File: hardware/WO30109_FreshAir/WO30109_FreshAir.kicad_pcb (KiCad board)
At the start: 2 copper layers, 63.4 x 83.1 mm, 44 parts, among them K1 G5Q-1 DC12, K2 G5Q-1 DC12, K3 G5Q-1 DC12, K4 G5Q-1 DC12, P1 AC IN, P2 SWD, P3 AC OUT, Q1 Si2302CDS, Q2 Si2302CDS, Q3 Si2302CDS, Q4 Si2302CDS, U1 STM32F103C8T6, U2 IRM-02-12, U3 ZS3L, U4 LM1117-3.3

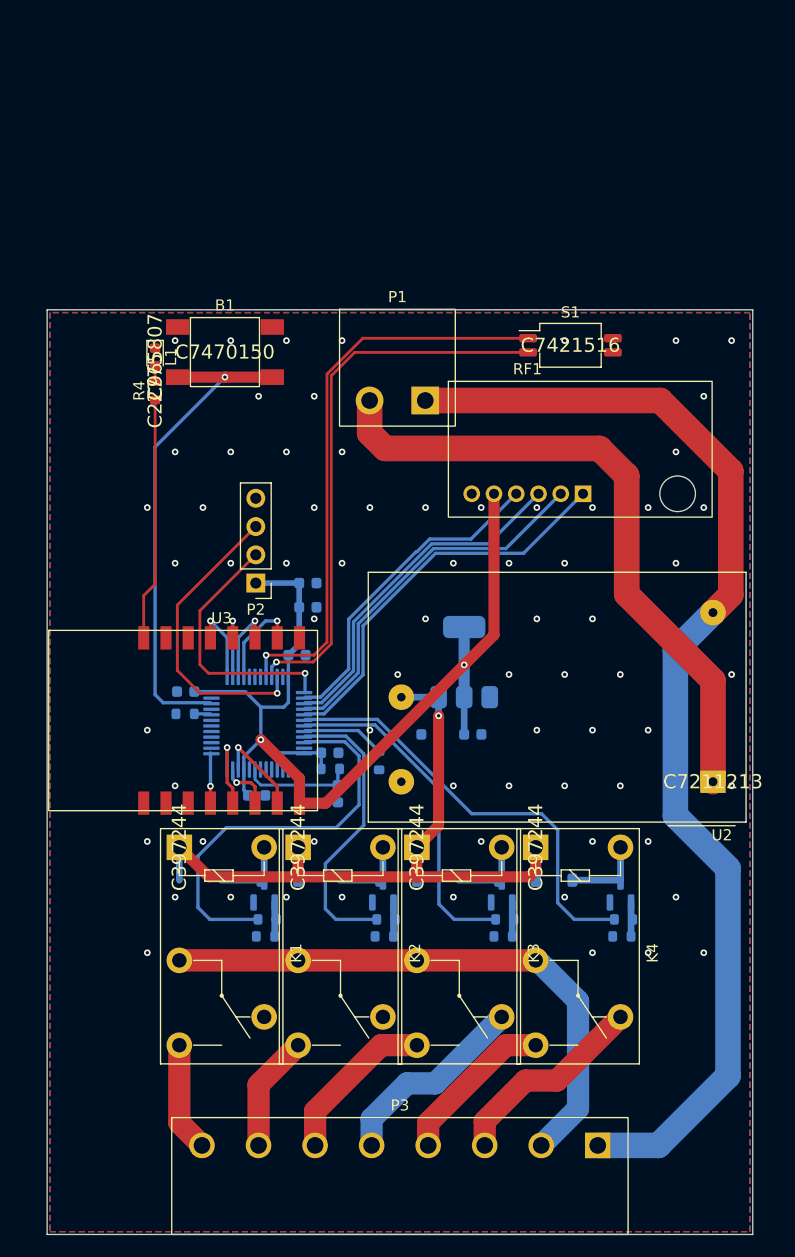
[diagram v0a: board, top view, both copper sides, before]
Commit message: feat(v2.0): PCB 安規改版完成 — DRC 0 錯誤、全部接通
PCB
- 市電↔低壓 ≥6.4mm、市電網路間 ≥1.5mm、板邊 ≥0.5mm（.kicad_dru 規則）
- 新增固定孔到市電 ≥2.3mm 規則；右緣市電走道外移、AC_N 在 H2 旁內彎（H2 0.85→2.85mm）
- F1/RV1、AP63203 降壓、繼電器驅動、RF1/P2/S1 重新擺放；H1–H4 固定孔
- 繼電器輸出 DO_* 由 mains_router 雙層格點佈線；低壓由 Freerouting，剩餘由 route_leftovers 補
- GND 鋪銅依規則自動退讓；LCSC 料號不印絲印

工具與文件
- scripts/build_v20.sh 一鍵重建（多組 Freerouting 設定，取第一組全接通）
- .github/workflows/kicad-ci.yml：ERC/DRC/生產檔
- README：架構、改版、安規、版控、CI、範例（mermaid 圖）＋板子圖片
- docs/review：V1.3 設計審查

驗證（kicad-cli 10.0.6）：ERC 0、DRC 0 錯誤、0 未連線、0 parity

Co-Authored-By: Claude Opus 5.5 (1M context) <noreply@anthropic.com>
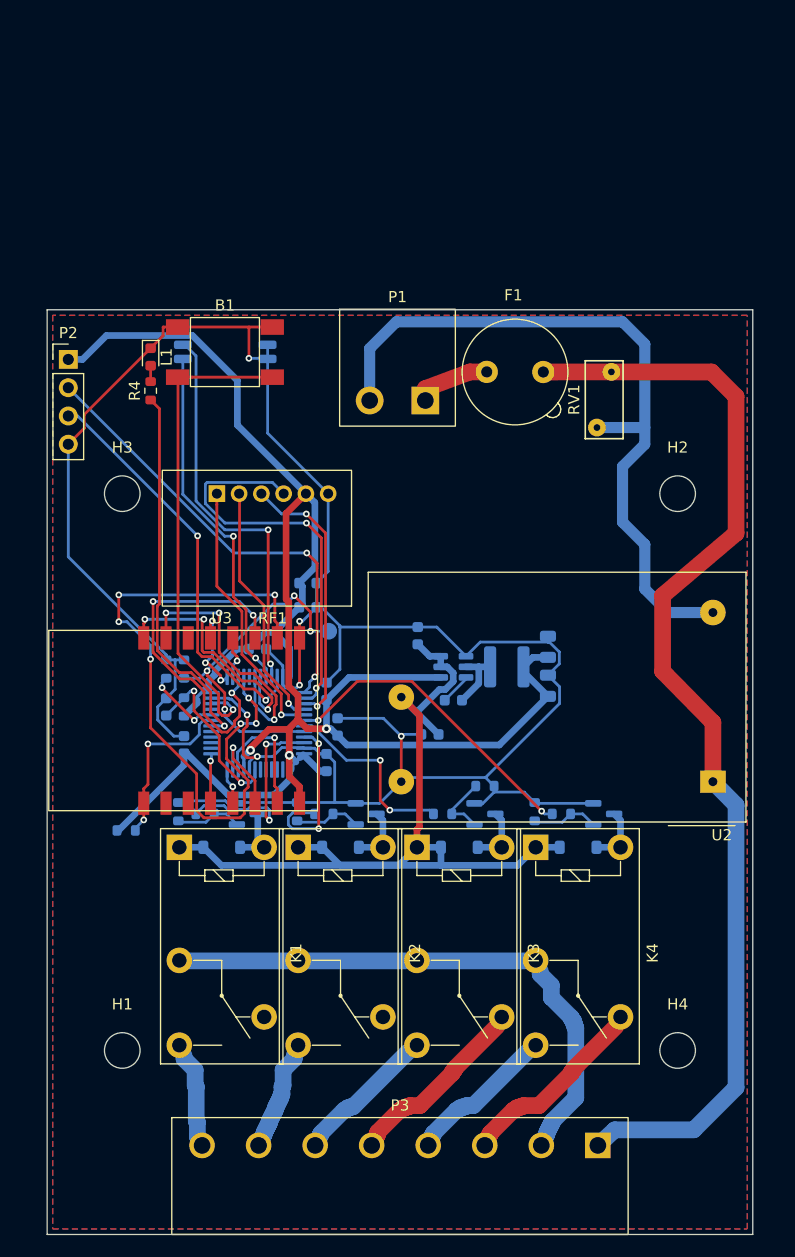
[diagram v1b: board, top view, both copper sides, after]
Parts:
- added C10: 1uF, Capacitor_SMD:C_0603_1608Metric, B.Cu at (112.3, 139.1)
- added C12: 100nF, Capacitor_SMD:C_0603_1608Metric, B.Cu at (136.5, 135.1)
- added C13: 22uF 25V, Capacitor_SMD:C_0805_2012Metric, B.Cu at (145.0, 130.3)
- added C14: 100nF, Capacitor_SMD:C_0603_1608Metric, B.Cu at (133.3, 129.3)
- added F1: T3.15A 250V, Fuse:Fuseholder_TR5_Littelfuse_No560_No460, F.Cu at (139.5, 105.6)
- added H1: M3, MountingHole:MountingHole_3.2mm_M3, F.Cu at (106.8, 166.6)
- added H2: M3, MountingHole:MountingHole_3.2mm_M3, F.Cu at (156.7, 116.5)
- added H3: M3, MountingHole:MountingHole_3.2mm_M3, F.Cu at (106.8, 116.5)
- added H4: M3, MountingHole:MountingHole_3.2mm_M3, F.Cu at (156.7, 166.6)
- added L2: 3.9uH, Inductor_SMD:L_Sunlord_SWPA4030S, B.Cu at (141.3, 132.1)
- added R13: 10k, Resistor_SMD:R_0603_1608Metric, B.Cu at (107.1, 146.8)
- added RV1: 07D471K, Varistor:RV_Disc_D7mm_W3.4mm_P5mm, F.Cu at (150.7, 105.6)
- added TP1: BOOT0, TestPoint:TestPoint_Pad_D1.5mm, B.Cu at (125.3, 128.9)
- C5: value 1uF -> 100nF
- C7: value 10uF -> 22uF 25V; footprint Capacitor_SMD:C_0603_1608Metric -> Capacitor_SMD:C_0805_2012Metric
- K1, K2, K3, K4: footprint Relay_THT:Relay_SPDT_Omron-G5Q-1 -> WOOW:Relay_SPDT_Omron-G5Q-1_Tight
- P1: value AC IN -> AC IN 230V
- S1: moved to B.Cu
- U4: value LM1117-3.3 -> AP63203WU-7; footprint Package_TO_SOT_SMD:SOT-223-3_TabPin2 -> Package_TO_SOT_SMD:TSOT-23-6
- moved S1 31.0 mm to (116.0, 103.8)
- moved P2 26.2 mm to (101.9, 104.5), turned to 0 degrees
- moved RF1 22.9 mm to (120.2, 116.5), turned to 180 degrees
- moved R2 19.4 mm to (112.3, 132.3), turned to 90 degrees
- moved C5 17.3 mm to (110.7, 135.7), turned to 90 degrees
- moved R1 14.3 mm to (112.3, 135.7), turned to 90 degrees
- moved C4 14.2 mm to (125.1, 140.7), turned to 90 degrees
- moved R10 13.7 mm to (122.5, 145.1), turned to 90 degrees
- moved R12 13.7 mm to (143.8, 145.1), turned to 90 degrees
- moved R9 13.7 mm to (111.8, 145.1), turned to 90 degrees
- moved R11 13.6 mm to (139.3, 142.8), turned to 0 degrees
- moved C3 11.3 mm to (125.1, 134.3), turned to 90 degrees
- moved R5 11.0 mm to (114.2, 145.3)
- moved R8 11.0 mm to (146.2, 145.3)
- moved R7 11.0 mm to (135.5, 145.3)
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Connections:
- P1 pad 1: /AC_L -> /AC_L_IN
- R4 pad 1: /NET_LED -> /LED
- U1 pad 18: unconnected-(U1-PB0-Pad18) -> /LED
- U1 pad 19: unconnected-(U1-PB1-Pad19) -> /ZB_RST
- U1 pad 30: unconnected-(U1-PA9-Pad30) -> /ZB_RX
- U1 pad 31: unconnected-(U1-PA10-Pad31) -> /ZB_TX
- U2 pad 1: /AC_N -> /AC_L
- U2 pad 2: /AC_L -> /AC_N
- U3 pad 1: unconnected-(U3-RST-Pad1) -> /ZB_RST
- U3 pad 15: unconnected-(U3-RXD-Pad15) -> /ZB_RX
- U3 pad 16: /NET_LED -> /ZB_TX
- U4 pad 1: /GND -> /+3V3
- U4 pad 2: /+3V3 -> /+12V
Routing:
- net /GND: track 0.00 -> 223.4 mm, vias 69 -> 6
- net /+3V3: track 93.1 -> 171.1 mm, vias 2 -> 3
- net /Input_1: track 8.23 -> 61.0 mm, vias 1 -> 7
- net /LED: track 0.00 -> 34.0 mm, vias 0 -> 1
- net /Input_2: track 7.00 -> 33.0 mm, vias 1 -> 3
- net /ZB_RX: track 0.00 -> 24.3 mm, vias 0 -> 3
- net /BOOT0: track 7.43 -> 30.9 mm, vias 0 -> 4
- net /ZB_TX: track 0.00 -> 22.5 mm, vias 0 -> 3
- net /NET_LED: track 21.8 -> 0.00 mm
- net /Mode_bit1: track 51.2 -> 32.2 mm, vias 1 -> 2
- net /Relay_1: track 36.6 -> 18.6 mm, vias 0 -> 2
- net /SWCLK: track 23.4 -> 41.0 mm, vias 1 -> 2
- net /ZB_RST: track 0.00 -> 15.4 mm, vias 0 -> 2
- net /Mode_bit0: track 49.6 -> 35.5 mm, vias 1 -> 2
- net /Relay_3: track 30.4 -> 17.0 mm, vias 0 -> 2
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
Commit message: feat: V2.0 設計驗證 — SPICE、PCB 計算器、熱、EMC、3D、kicadiff、Jobset
- docs/verification/README.md：13 項驗證總表與逐項結果
- sim/：ngspice 繼電器驅動（含拿掉續流二極體對照組）、LED 電流；CI 守門 Vds < 20V
- GND 縫合過孔 90 顆（DRC 仍 0）
- 自訂零件 3D 模型（OCP 產生 STEP）＋ assign_3d.py；正面最高 16.9mm
- .kicad_jobset：KiCad 原生一鍵產出 8/8 成功
- .kicad_pro MAINS 間距與 .kicad_dru 一致（1.5mm）
- 發現：市電 1.5mm 線 1oz 銅載流 3.21A ≈ 保險絲 3.15A，>3A 須 2oz

驗證（kicad-cli 10.0.6）：ERC 0、DRC 0 錯誤、0 未連線、0 parity

Co-Authored-By: Claude Opus 5.5 (1M context) <noreply@anthropic.com>
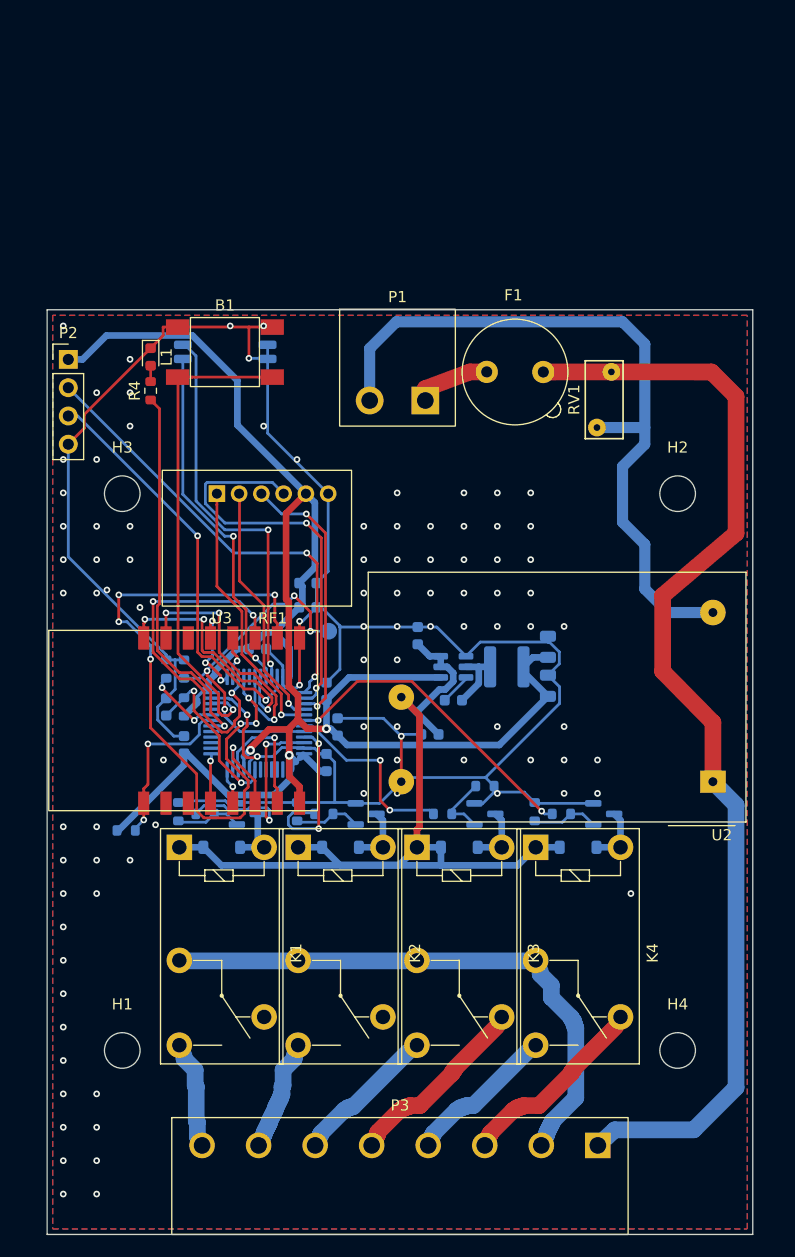
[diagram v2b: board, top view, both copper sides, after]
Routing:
- net /GND: vias 6 -> 96

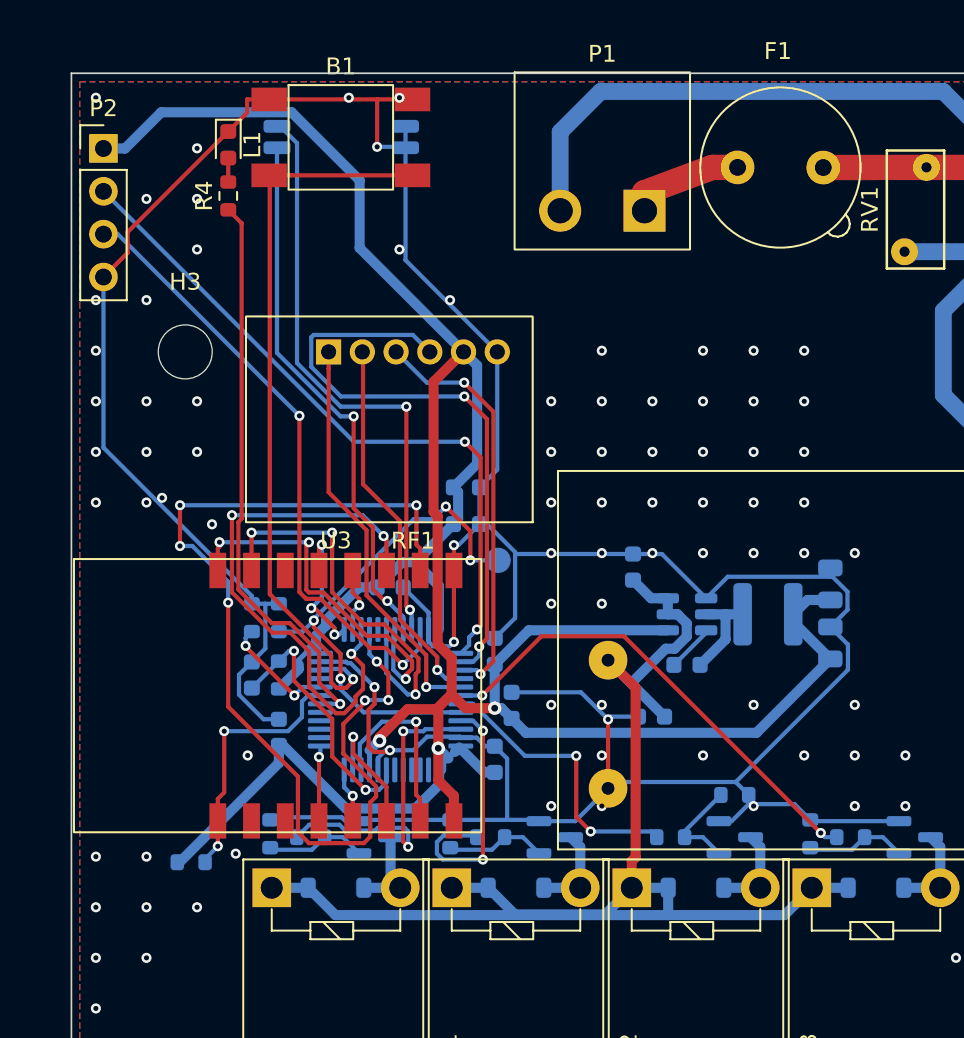
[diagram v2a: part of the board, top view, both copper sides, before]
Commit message: feat(v3.0): Tuya ZS3L＋EPA09-4D → ESP32-C6 單晶片＋SYN480R
- U1 STM32F103＋U3 ZS3L → ESP32-C6-WROOM-1-N8（C5366877，Zigbee 3.0，JLC 有庫存）
- RF1 EPA09-4D → SYN480R（C916347）＋13.52127MHz 晶振＋LC 匹配，韌體解 EV1527
- B1 改 IO9（BOOT），P2 改 2×3 燒錄座；ANT1 433MHz 天線焊點
- PCB 從 v2.0 標籤開始，只動低壓區；build_v30.sh 一鍵重建
- 檢查：ERC 0 錯誤、DRC 0 錯誤、0 未連線、parity 0

Co-Authored-By: Claude Opus 5.5 (1M context) <noreply@anthropic.com>
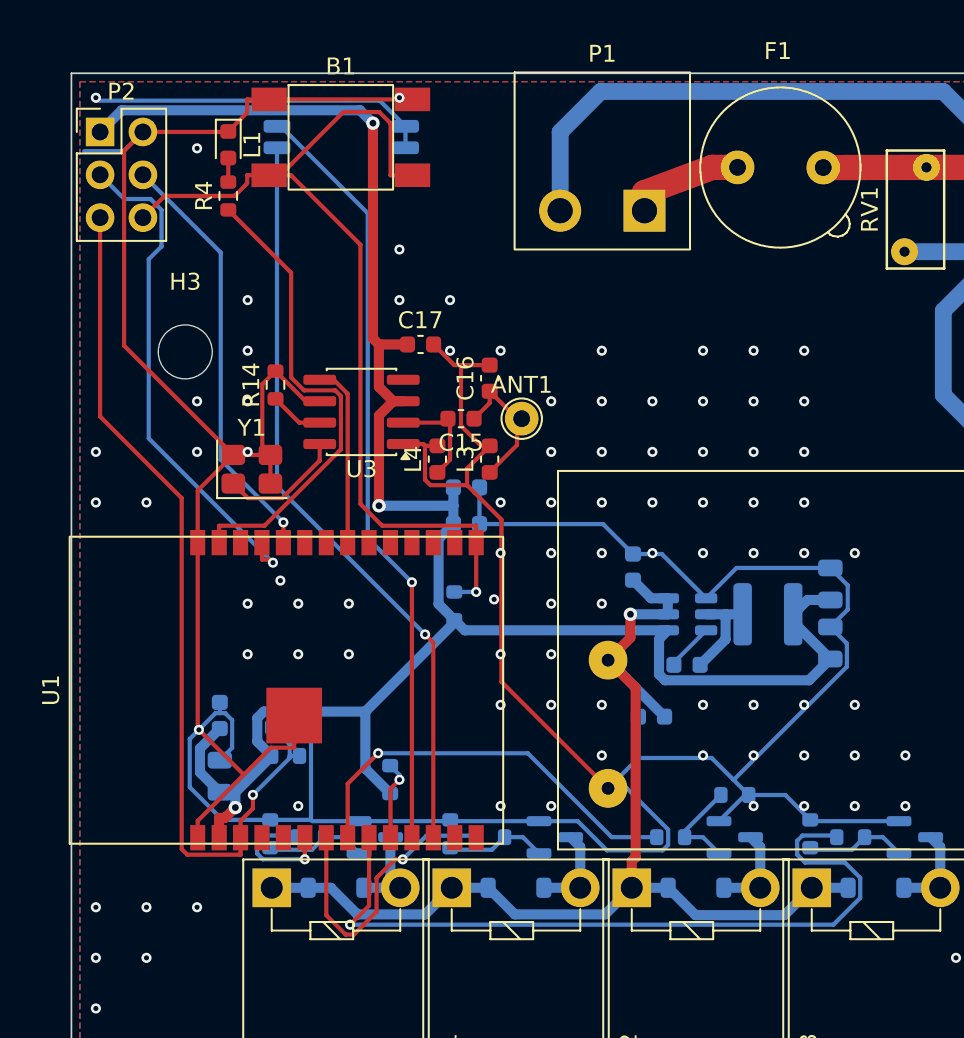
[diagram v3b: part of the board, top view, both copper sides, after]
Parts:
- removed C10: 1uF, Capacitor_SMD:C_0603_1608Metric
- removed C3, C4: 100nF, Capacitor_SMD:C_0603_1608Metric
- removed R13: 10k, Resistor_SMD:R_0603_1608Metric
- removed RF1: EPA09-4D, WOOW:Ebelong_EPA09-4D
- removed TP1: BOOT0, TestPoint:TestPoint_Pad_D1.5mm
- added ANT1: 433MHz 1/4λ 17.3cm, TestPoint:TestPoint_THTPad_D2.0mm_Drill1.0mm, F.Cu at (126.7, 120.5)
- added C15: 6.8pF C0G, Capacitor_SMD:C_0603_1608Metric, F.Cu at (123.1, 120.5)
- added C16: 1.8pF C0G, Capacitor_SMD:C_0603_1608Metric, F.Cu at (124.8, 118.1)
- added C17: 1uF, Capacitor_SMD:C_0603_1608Metric, F.Cu at (120.7, 116.1)
- added L3: 27nH, Inductor_SMD:L_0603_1608Metric, F.Cu at (124.8, 122.9)
- added L4: 47nH, Inductor_SMD:L_0603_1608Metric, F.Cu at (121.7, 122.9)
- added R14: 0R, Resistor_SMD:R_0603_1608Metric, F.Cu at (112.1, 118.5)
- added Y1: 13.52127MHz 20pF, Crystal:Crystal_SMD_3225-4Pin_3.2x2.5mm, F.Cu at (110.7, 123.5)
- C1: value 100nF -> 22uF 25V; footprint Capacitor_SMD:C_0603_1608Metric -> Capacitor_SMD:C_0805_2012Metric
- C5: value 100nF -> 1uF
- P2: value SWD -> PROG; footprint Connector_PinHeader_2.54mm:PinHeader_1x04_P2.54mm_Vertical -> Connector_PinHeader_2.54mm:PinHeader_2x03_P2.54mm_Vertical
- R2, R3: value 100k -> 10k
- U1: value STM32F103C8T6 -> ESP32-C6-WROOM-1-N8; footprint Package_QFP:LQFP-48_7x7mm_P0.5mm -> WOOW:Espressif_ESP32-C6-WROOM-1; moved to F.Cu
- U3: value ZS3L -> SYN480R; footprint WOOW:Tuya_ZS3L -> Package_SO:SOIC-8_3.9x4.9mm_P1.27mm
- moved C2 17.3 mm to (108.8, 138.1)
- moved U3 16.9 mm to (117.2, 120.1), turned to 180 degrees
- moved C1 15.1 mm to (108.8, 141.7), turned to 90 degrees
- moved R3 12.6 mm to (118.9, 141.9)
- moved R2 10.4 mm to (122.7, 131.6)
- moved U1 6.20 mm to (112.8, 136.6)
- moved R1 4.82 mm to (112.7, 140.5), turned to 0 degrees
- moved C5 3.69 mm to (112.7, 138.8), turned to 0 degrees
- moved P2 1.00 mm to (101.7, 103.5)
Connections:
- B1 pad 2: /Reset_Button -> /BOOT
- C5 pad 1: /NRST -> /EN
- P2 pad 2: /SWCLK -> /GND
- P2 pad 3: /SWDIO -> /U0TXD
- P2 pad 4: /GND -> /U0RXD
- R1 pad 2: /NRST -> /EN
- R2 pad 1: /BOOT0 -> /+3V3
- R2 pad 2: /GND -> /BOOT
- R3 pad 1: /BOOT1 -> /+3V3
- R3 pad 2: /GND -> /IO8
- U1 pad 1: /+3V3 -> /GND
- U1 pad 10: /Output_1 -> /IO8
- U1 pad 11: /Output_2 -> /Mode_bit0
- U1 pad 12: /Output_3 -> /Mode_bit1
- U1 pad 13: /Output_4 -> unconnected-(U1-IO12/USB_D--Pad13)
- U1 pad 15: unconnected-(U1-PA5-Pad15) -> /BOOT
- U1 pad 18: /LED -> unconnected-(U1-IO20-Pad18)
- U1 pad 19: /ZB_RST -> unconnected-(U1-IO21-Pad19)
- U1 pad 2: unconnected-(U1-PC13-Pad2) -> /+3V3
- U1 pad 20: /BOOT1 -> unconnected-(U1-IO22-Pad20)
- U1 pad 21: unconnected-(U1-PB10-Pad21) -> /RF_DATA
- U1 pad 22: /Reset_Button -> unconnected-(U1-NC-Pad22)
- U1 pad 23: /GND -> unconnected-(U1-IO15-Pad23)
- U1 pad 24: /+3V3 -> /U0RXD
- U1 pad 25: /Input_4 -> /U0TXD
- U1 pad 26: /Input_3 -> unconnected-(U1-IO3-Pad26)
- U1 pad 27: /Input_2 -> /LED
- U1 pad 28: /Input_1 -> /GND
- U1 pad 29: unconnected-(U1-PA8-Pad29) -> /GND
- U1 pad 3: unconnected-(U1-PC14-Pad3) -> /EN
- U1 pad 6: unconnected-(U1-PD1-Pad6) -> /Relay_1
- U1 pad 7: /NRST -> /Relay_2
- U1 pad 8: /GND -> /Relay_3
- U1 pad 9: /+3V3 -> /Relay_4
- U3 pad 1: /ZB_RST -> /GND
- U3 pad 2: unconnected-(U3-ADC_PC01-Pad2) -> /RF_IN
- U3 pad 3: unconnected-(U3-NC-Pad3) -> /+3V3
- U3 pad 4: /Output_4 -> unconnected-(U3-NC-Pad4)
- U3 pad 5: /Output_3 -> /RF_DATA
- U3 pad 6: /Output_2 -> /GND
- U3 pad 7: /Output_1 -> /RF_SQ
- U3 pad 8: /+3V3 -> /RF_XTAL
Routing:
- net /Input_1: track 61.0 -> 0.00 mm, vias 7 -> 0
- net /BOOT: track 0.00 -> 56.7 mm, vias 0 -> 1
- net /EN: track 0.00 -> 52.8 mm, vias 0 -> 1
- net /+3V3: track 171.1 -> 122.8 mm
- net /Reset_Button: track 44.1 -> 0.00 mm, vias 1 -> 0
- net /GND: track 223.4 -> 265.8 mm, vias 96 -> 100
- net /SWCLK: track 41.0 -> 0.00 mm, vias 2 -> 0
- net /SWDIO: track 37.0 -> 0.00 mm, vias 2 -> 0
- net /RF_4: track 36.4 -> 0.00 mm, vias 2 -> 0
- net /Input_2: track 33.0 -> 0.00 mm, vias 3 -> 0
- net /BOOT0: track 30.9 -> 0.00 mm, vias 4 -> 0
- net /U0TXD: track 0.00 -> 30.5 mm, vias 0 -> 1
- net /U0RXD: track 0.00 -> 25.3 mm, vias 0 -> 1
- net /RF_3: track 24.4 -> 0.00 mm, vias 2 -> 0
- net /ZB_RX: track 24.3 -> 0.00 mm, vias 3 -> 0
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
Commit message: hw: V3.1 433 匹配重新選值、續流改 B5819W（只換值不改佈線）
- C15/C16 2.7pF（C162221）、L3 47nH（C29683）、L4 33nH（C35050）：規格書值以同系列
  Micrel 原廠輸入阻抗算峰值在 210–230MHz，新值 433.92MHz 失配 8–13dB → 3.1–5.3dB
- D1–D4 1N4148W → B5819W（C8598，基礎料、同 SOD-123），配合 PWM 保持（Vf ≤0.4V）
- sim/rf_match.cir 改用原廠阻抗、新舊值並排；scripts/rf_match_opt.py 最差情況選值
- jlc_footprints.json 補新料號、刪舊料號；--refresh-footprints 預設只抓缺的
- ERC 0、DRC 0、parity 0

Co-Authored-By: Claude Opus 5.5 (1M context) <noreply@anthropic.com>
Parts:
- C15: value 6.8pF C0G -> 2.7pF C0G
- C16: value 1.8pF C0G -> 2.7pF C0G
- D1, D2, D3, D4: value 1N4148W -> B5819W
- L3: value 27nH -> 47nH
- L4: value 47nH -> 33nH
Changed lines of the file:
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@@
 	)
 	(paper "A4")
+	(title_block
+		(rev "3.1")
+	)
 	(layers
 		(0 "F.Cu" signal)
@@
 			)
 		)
-		(property "Value" "1.8pF C0G"
+		(property "Value" "2.7pF C0G"
 			(at 0 1.43 90)
 			(layer "F.Fab")
@@
 			)
 		)
-		(property "LCSC" "C1640"
+		(property "LCSC" "C162221"
 			(at 0 0 90)
 			(layer "F.Fab")
@@
 			)
 		)
-		(property "Value" "6.8pF C0G"
+		(property "Value" "2.7pF C0G"
 			(at 0 1.43 180)
 			(layer "F.Fab")
@@
 			)
 		)
-		(property "LCSC" "C1679"
+		(property "LCSC" "C162221"
 			(at 0 0 180)
 			(layer "F.Fab")
@@
 			)
 		)
-		(property "Value" "47nH"
+		(property "Value" "33nH"
 			(at 0 1.43 90)
 			(layer "F.Fab")
@@
 			)
 		)
-		(property "LCSC" "C29683"
+		(property "LCSC" "C35050"
 			(at 0 0 90)
 			(layer "F.Fab")
@@
 			)
 		)
-		(property "Value" "27nH"
+		(property "Value" "47nH"
 			(at 0 1.43 90)
 			(layer "F.Fab")
@@
 			)
 		)
-		(property "LCSC" "C12100"
+		(property "LCSC" "C29683"
 			(at 0 0 90)
 			(layer "F.Fab")
@@
 			)
 		)
-		(property "Value" "1N4148W"
+		(property "Value" "B5819W"
 			(at 0 -2.1 180)
 			(layer "B.Fab")
@@
 			)
 		)
-		(property "LCSC" "C81598"
+		(property "LCSC" "C8598"
 			(at 0 0 0)
 			(layer "F.Fab")
@@
 			)
 		)
-		(property "Value" "1N4148W"
+		(property "Value" "B5819W"
 			(at 0 -2.1 180)
 			(layer "B.Fab")
@@
 			)
 		)
-		(property "LCSC" "C81598"
+		(property "LCSC" "C8598"
 			(at 0 0 0)
 			(layer "F.Fab")
@@
 			)
 		)
-		(property "Value" "1N4148W"
+		(property "Value" "B5819W"
 			(at 0 -2.1 180)
 			(layer "B.Fab")
@@
 			)
 		)
-		(property "LCSC" "C81598"
+		(property "LCSC" "C8598"
 			(at 0 0 0)
 			(layer "F.Fab")
@@
 			)
 		)
-		(property "Value" "1N4148W"
+		(property "Value" "B5819W"
 			(at 0 -2.1 180)
 			(layer "B.Fab")
@@
 			)
 		)
-		(property "LCSC" "C81598"
+		(property "LCSC" "C8598"
 			(at 0 0 0)
 			(layer "F.Fab")
